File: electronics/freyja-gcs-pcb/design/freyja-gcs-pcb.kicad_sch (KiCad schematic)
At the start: 32 parts, among them J1 Conn_01x07_Pin, J2 GT-USB-7010ASV, SW1 SW_SPST, SW2 SW_SPST, U1 SN65HVD232DR, U2 STM32U575RGTx, Y1 48MHz, Y2 32768Hz

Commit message: 7 segment display
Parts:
- removed D3: LED Green, symbol Device:LED
- removed R3: 470, symbol Device:R
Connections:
- net 7SEG_SHCLK: now reaches U2.14 (PA0)
- net 7SEG_STCLK: now reaches U2.15 (PA1)
- net 7SEG_DA: now reaches U2.16 (PA2)
- net 7SEG_DIG1: now reaches U2.17 (PA3)
- net 7SEG_DIG2: now reaches U2.20 (PA4)
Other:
- sheet Switch_pins renamed Switches
- added sheet 7-Segment Display (7seg.kicad_sch)

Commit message: global reset
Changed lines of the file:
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@@
-	(wire
-		(pts
-			(xy 55.88 40.64) (xy 60.96 40.64)
-		)
-		(stroke
-			(width 0)
-			(type default)
-		)
-	)
 	(wire
 		(pts
@@
 		(pts
 			(xy 76.2 33.02) (xy 76.2 31.75)
+		)
+		(stroke
+			(width 0)
+			(type default)
+		)
+	)
+	(wire
+		(pts
+			(xy 59.69 40.64) (xy 60.96 40.64)
 		)
 		(stroke
@@
 	(label "USB_D_P"
 		(at 36.83 167.64 0)
-		(effects
-			(font
-				(size 1.27 1.27)
-			)
-			(justify left bottom)
-		)
-	)
-	(label "NRST"
-		(at 55.88 40.64 0)
 		(effects
 			(font
@@
 				(hide yes)
 			)
+		)
+	)
+	(global_label "NRST"
+		(shape output)
+		(at 59.69 40.64 180)
+		(fields_autoplaced yes)
+		(effects
+			(font
+				(size 1.27 1.27)
+			)
+			(justify right)
+		)
+		(property "Intersheetrefs" "${INTERSHEET_REFS}"
+			(at 51.9272 40.64 0)
+			(effects
+				(font
+					(size 1.27 1.27)
+				)
+				(justify right)
+				(hide yes)
+			)

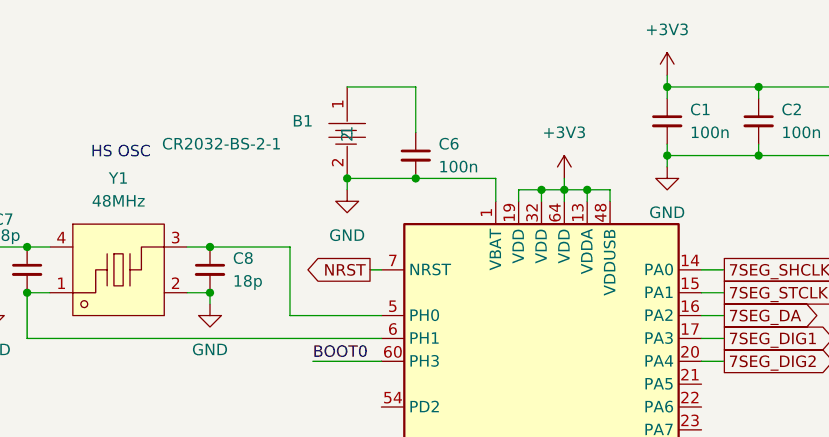
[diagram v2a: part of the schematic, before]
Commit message: fix cr2032 short circuit
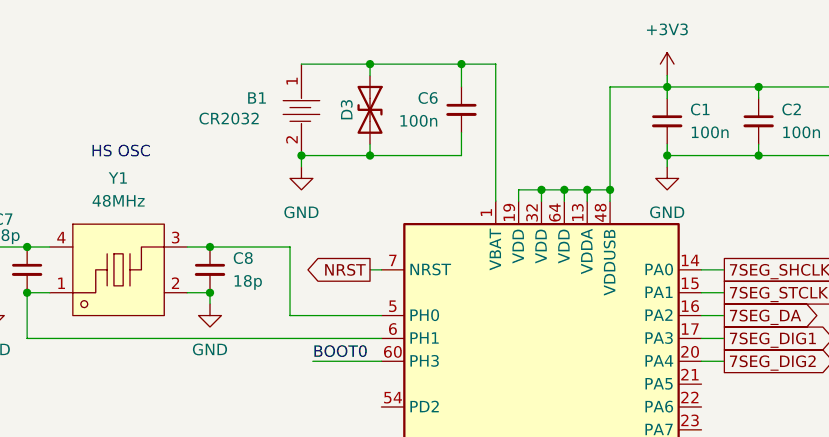
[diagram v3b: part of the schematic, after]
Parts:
- added D3: 0603ESDA-05N, Diode_SMD:D_0603_1608Metric_Pad1.05x0.95mm_HandSolder, symbol Device:D_TVS
- B1: value CR2032-BS-2-1 -> CR2032
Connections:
- net GND: now also D3.2 (A2); no longer U2.1 (VBAT)
- net at B1.1, C6.1: now also U2.1 (VBAT), D3.1 (A1)
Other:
- moved on the sheet: C6
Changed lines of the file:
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@@
 	)
 	(junction
-		(at 64.77 30.48)
+		(at 81.28 31.75)
 		(diameter 0)
 		(color 0 0 0 0)
 	)
 	(junction
-		(at 81.28 31.75)
+		(at 59.69 27.94)
+		(diameter 0)
+		(color 0 0 0 0)
+	)
+	(junction
+		(at 59.69 17.78)
 		(diameter 0)
 		(color 0 0 0 0)
@@
 	)
 	(junction
+		(at 69.85 17.78)
+		(diameter 0)
+		(color 0 0 0 0)
+	)
+	(junction
 		(at 41.91 38.1)
 		(diameter 0)
@@
 	)
 	(junction
+		(at 86.36 31.75)
+		(diameter 0)
+		(color 0 0 0 0)
+	)
+	(junction
 		(at 168.91 45.72)
 		(diameter 0)
@@
 	)
 	(junction
-		(at 57.15 30.48)
+		(at 52.07 27.94)
 		(diameter 0)
 		(color 0 0 0 0)
@@
 	(wire
 		(pts
-			(xy 73.66 33.02) (xy 73.66 30.48)
+			(xy 86.36 20.32) (xy 86.36 31.75)
+		)
+		(stroke
+			(width 0)
+			(type default)
+		)
+	)
+	(wire
+		(pts
+			(xy 73.66 17.78) (xy 73.66 33.02)
 		)
 		(stroke
@@
 	(wire
 		(pts
+			(xy 86.36 20.32) (xy 92.71 20.32)
+		)
+		(stroke
+			(width 0)
+			(type default)
+		)
+	)
+	(wire
+		(pts
 			(xy 123.19 20.32) (xy 123.19 21.59)
 		)
@@
 	(wire
 		(pts
+			(xy 59.69 17.78) (xy 52.07 17.78)
+		)
+		(stroke
+			(width 0)
+			(type default)
+		)
+	)
+	(wire
+		(pts
 			(xy 26.67 167.64) (xy 27.94 167.64)
 		)
@@
 	(wire
 		(pts
+			(xy 69.85 25.4) (xy 69.85 27.94)
+		)
+		(stroke
+			(width 0)
+			(type default)
+		)
+	)
+	(wire
+		(pts
 			(xy 36.83 106.68) (xy 43.18 106.68)
 		)
@@
 	(wire
 		(pts
-			(xy 73.66 30.48) (xy 64.77 30.48)
-		)
-		(stroke
-			(width 0)
-			(type default)
-		)
-	)
-	(wire
-		(pts
 			(xy 92.71 168.91) (xy 100.33 168.91)
 		)
@@
 	(wire
 		(pts
-			(xy 57.15 30.48) (xy 64.77 30.48)
+			(xy 52.07 27.94) (xy 59.69 27.94)
 		)
 		(stroke
@@
 	(wire
 		(pts
-			(xy 64.77 25.4) (xy 64.77 20.32)
+			(xy 69.85 17.78) (xy 69.85 20.32)
 		)
 		(stroke
@@
 	(wire
 		(pts
-			(xy 81.28 30.48) (xy 81.28 31.75)
+			(xy 59.69 26.67) (xy 59.69 27.94)
+		)
+		(stroke
+			(width 0)
+			(type default)
+		)
+	)
+	(wire
+		(pts
+			(xy 59.69 17.78) (xy 59.69 19.05)
+		)
+		(stroke
+			(width 0)
+			(type default)
+		)
+	)
+	(wire
+		(pts
+			(xy 69.85 17.78) (xy 73.66 17.78)
 		)
 		(stroke
@@
 	(wire
 		(pts
-			(xy 64.77 20.32) (xy 57.15 20.32)
+			(xy 59.69 17.78) (xy 69.85 17.78)
 		)
 		(stroke
@@
 	(wire
 		(pts
+			(xy 59.69 27.94) (xy 69.85 27.94)
+		)
+		(stroke
+			(width 0)
+			(type default)
+		)
+	)
+	(wire
+		(pts
 			(xy 179.07 54.61) (xy 179.07 55.88)
 		)
@@
 	(wire
 		(pts
-			(xy 57.15 30.48) (xy 57.15 31.75)
+			(xy 52.07 27.94) (xy 52.07 29.21)
 		)
 		(stroke
@@
 	(symbol
 		(lib_id "power:GND")
-		(at 57.15 31.75 0)
+		(at 52.07 29.21 0)
 		(unit 1)
 		(exclude_from_sim no)
@@
 		(fields_autoplaced yes)
 		(property "Reference" "#PWR05"
-			(at 57.15 38.1 0)
+			(at 52.07 35.56 0)
 			(effects
 				(font
@@
 		)
 		(property "Value" "GND"
-			(at 57.15 36.83 0)
+			(at 52.07 34.29 0)
 			(effects
 				(font
@@
 		)
 		(property "Footprint" ""
-			(at 57.15 31.75 0)
+			(at 52.07 29.21 0)
 			(effects
 				(font
@@
 		)
 		(property "Datasheet" ""
-			(at 57.15 31.75 0)
+			(at 52.07 29.21 0)
 			(effects
 				(font
@@
 		)
 		(property "Description" "Power symbol creates a global label with name \"GND\" , ground"
-			(at 57.15 31.75 0)
+			(at 52.07 29.21 0)
 			(effects
 				(font
@@
 	(symbol
 		(lib_id "EasyEDA:CR2032-BS-2-1")
-		(at 57.15 25.4 270)
+		(at 52.07 22.86 270)
 		(unit 1)
 		(exclude_from_sim no)
@@
 		(dnp no)
 		(property "Reference" "B1"
-			(at 51.054 24.13 90)
+			(at 45.974 21.59 90)
 			(effects
 				(font
@@
 			)
 		)
-		(property "Value" "CR2032-BS-2-1"
-			(at 36.576 26.67 90)
+		(property "Value" "CR2032"
+			(at 40.64 23.876 90)
 			(effects
 				(font
@@
 		)
 		(property "Footprint" "EasyEDA:BAT-TH_BS-2-1"
-			(at 49.53 25.4 0)
+			(at 44.45 22.86 0)
 			(effects
 				(font
@@
 		)
 		(property "Datasheet" "https://lcsc.com/product-detail/Battery-Holders-Clips-Contacts_CR2032battery_C70376.html"
-			(at 46.99 25.4 0)
+			(at 41.91 22.86 0)
 			(effects
 				(font
@@
 			)
 		)
-		(property "Description" ""
-			(at 57.15 25.4 0)
+		(property "Description" "CR2032-BS-2-1"
+			(at 52.07 22.86 0)
 			(effects
 				(font
@@
 		)
 		(property "LCSC Part" "C70376"
-			(at 44.45 25.4 0)
+			(at 39.37 22.86 0)
 			(effects
 				(font
@@
 	)
 	(symbol
+		(lib_id "Device:D_TVS")
+		(at 59.69 22.86 270)
+		(unit 1)
+		(exclude_from_sim no)
+		(in_bom yes)
+		(on_board yes)
+		(dnp no)
+		(property "Reference" "D3"
+			(at 57.15 22.86 0)
+			(effects
+				(font
+					(size 1.27 1.27)
+				)
+			)
+		)
+		(property "Value" "0603ESDA-05N"
+			(at 57.15 21.5901 90)
+			(effects
+				(font
+					(size 1.27 1.27)
+				)
+				(justify right)
+				(hide yes)
+			)
+		)
+		(property "Footprint" "Diode_SMD:D_0603_1608Metric_Pad1.05x0.95mm_HandSolder"
+			(at 59.69 22.86 0)
+			(effects
+				(font
+					(size 1.27 1.27)
+				)
+				(hide yes)
+			)
+		)
+		(property "Datasheet" "~"
+			(at 59.69 22.86 0)
+			(effects
+				(font
+					(size 1.27 1.27)
+				)
+				(hide yes)
+			)
+		)
+		(property "Description" "Bidirectional transient-voltage-suppression diode"
+			(at 59.69 22.86 0)
+			(effects
+				(font
+					(size 1.27 1.27)
+				)
+				(hide yes)
+			)
+		)
+		(property "LCSC Part" "C316054"
+			(at 46.99 22.86 0)
+			(effects
+				(font
+					(size 1.27 1.27)
+				)
+				(hide yes)
+			)
+		)
+		(pin "1"
+		)
+		(pin "2"
+		)
+		(instances
+			(project "freyja-gcs-pcb"
+				(path "/c292fa04-82ad-49e9-a9d8-422554d1d11d"
+					(reference "D3")
+					(unit 1)
+				)
+			)
+		)
+	)
+	(symbol
 		(lib_id "Device:R")
 		(at 31.75 157.48 90)
@@
 	(symbol
 		(lib_id "Device:C_Small")
-		(at 64.77 27.94 0)
+		(at 69.85 22.86 0)
+		(mirror y)
 		(unit 1)
 		(exclude_from_sim no)
@@
 		(on_board yes)
 		(dnp no)
-		(fields_autoplaced yes)
 		(property "Reference" "C6"
-			(at 67.31 26.6762 0)
+			(at 67.31 21.59 0)
 			(effects
 				(font
@@
 		)
 		(property "Value" "100n"
-			(at 67.31 29.2162 0)
+			(at 67.31 24.13 0)
 			(effects
 				(font
@@
 		)
 		(property "Footprint" ""
-			(at 64.77 27.94 0)
+			(at 69.85 22.86 0)
 			(effects
 				(font
@@
 		)
 		(property "Datasheet" "~"
-			(at 64.77 27.94 0)
+			(at 69.85 22.86 0)
 			(effects
 				(font
@@
 		)
 		(property "Description" "Unpolarized capacitor, small symbol"
-			(at 64.77 27.94 0)
+			(at 69.85 22.86 0)
 			(effects
 				(font
@@
 					(unit 1)
 				)
-			)
-		)
-	)
-	(symbol
-		(lib_id "power:+3V3")
-		(at 81.28 30.48 0)
-		(unit 1)
-		(exclude_from_sim no)
-		(in_bom yes)
-		(on_board yes)
-		(dnp no)
-		(fields_autoplaced yes)
-		(property "Reference" "#PWR03"
-			(at 81.28 34.29 0)
-			(effects
-				(font
-					(size 1.27 1.27)
-				)
-				(hide yes)
-			)
-		)
-		(property "Value" "+3V3"
-			(at 81.28 25.4 0)
-			(effects
-				(font
-					(size 1.27 1.27)
-				)
-			)
-		)
-		(property "Footprint" ""
-			(at 81.28 30.48 0)
-			(effects
-				(font
-					(size 1.27 1.27)
-				)
-				(hide yes)
-			)
-		)
-		(property "Datasheet" ""
-			(at 81.28 30.48 0)
-			(effects
-				(font
-					(size 1.27 1.27)
-				)
-				(hide yes)
-			)
-		)
-		(property "Description" "Power symbol creates a global label with name \"+3V3\""
-			(at 81.28 30.48 0)
-			(effects
-				(font
-					(size 1.27 1.27)
-				)
-				(hide yes)
-			)
-		)
-		(pin "1"
-		)
-		(instances
-			(project ""
-				(path "/c292fa04-82ad-49e9-a9d8-422554d1d11d"
-					(reference "#PWR03")
-					(unit 1)
-				)

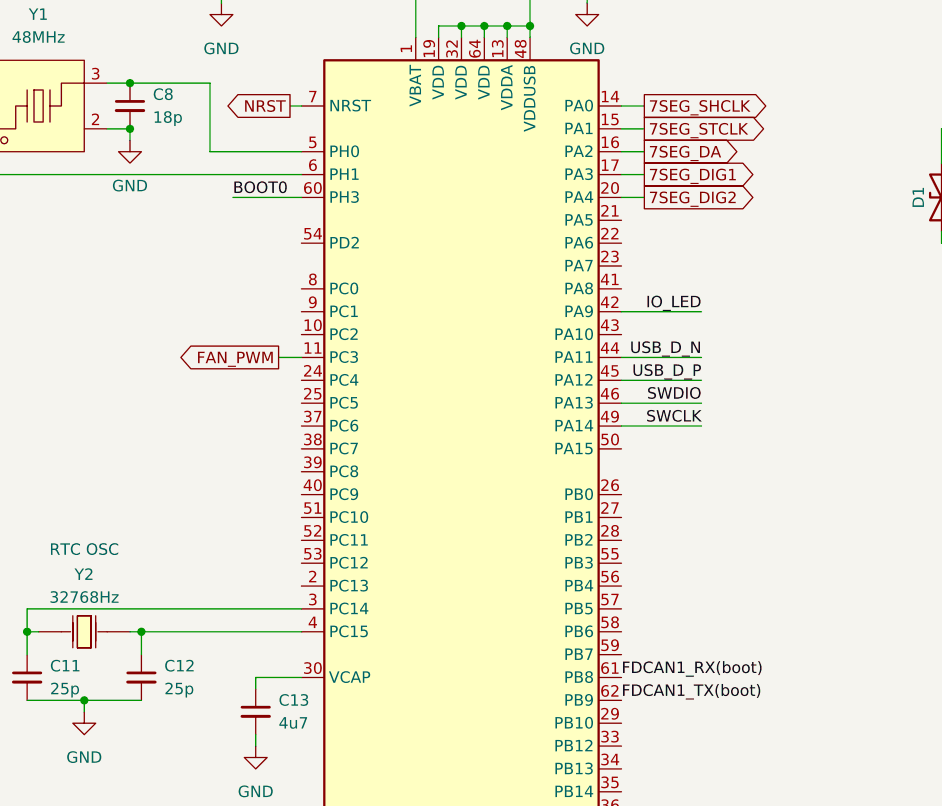
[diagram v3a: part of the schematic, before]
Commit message: change pwm channels
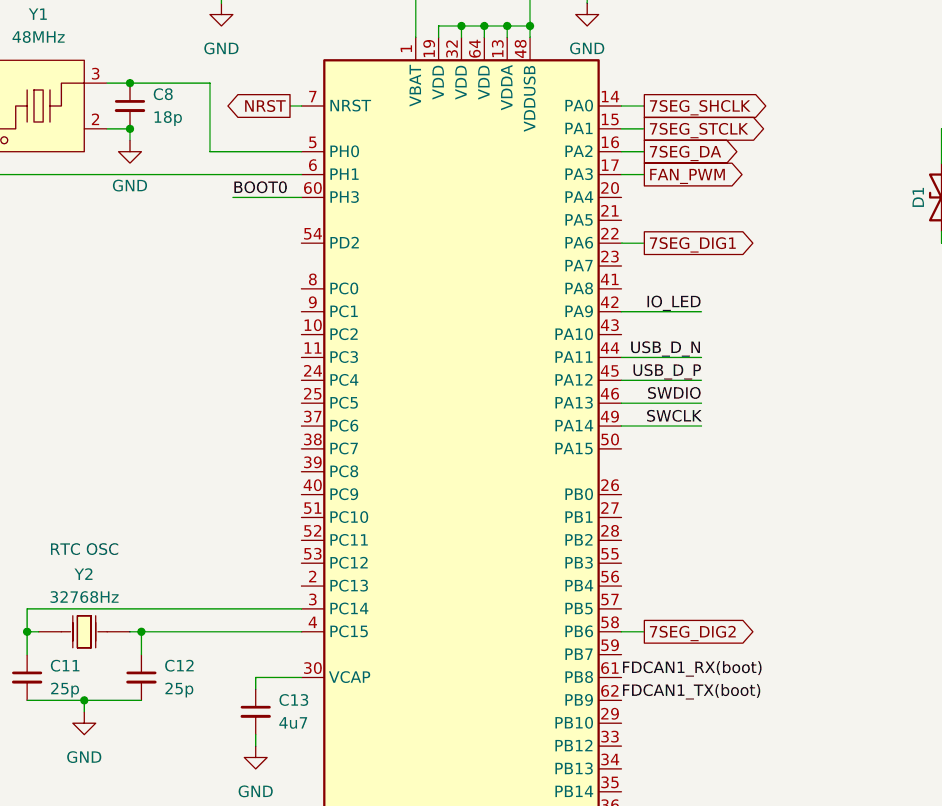
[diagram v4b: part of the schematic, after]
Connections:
- net 7SEG_DIG1: now also U2.22 (PA6); no longer U2.17 (PA3)
- net 7SEG_DIG2: now also U2.58 (PB6); no longer U2.20 (PA4)
- net FAN_PWM: now also U2.17 (PA3); no longer U2.11 (PC3)

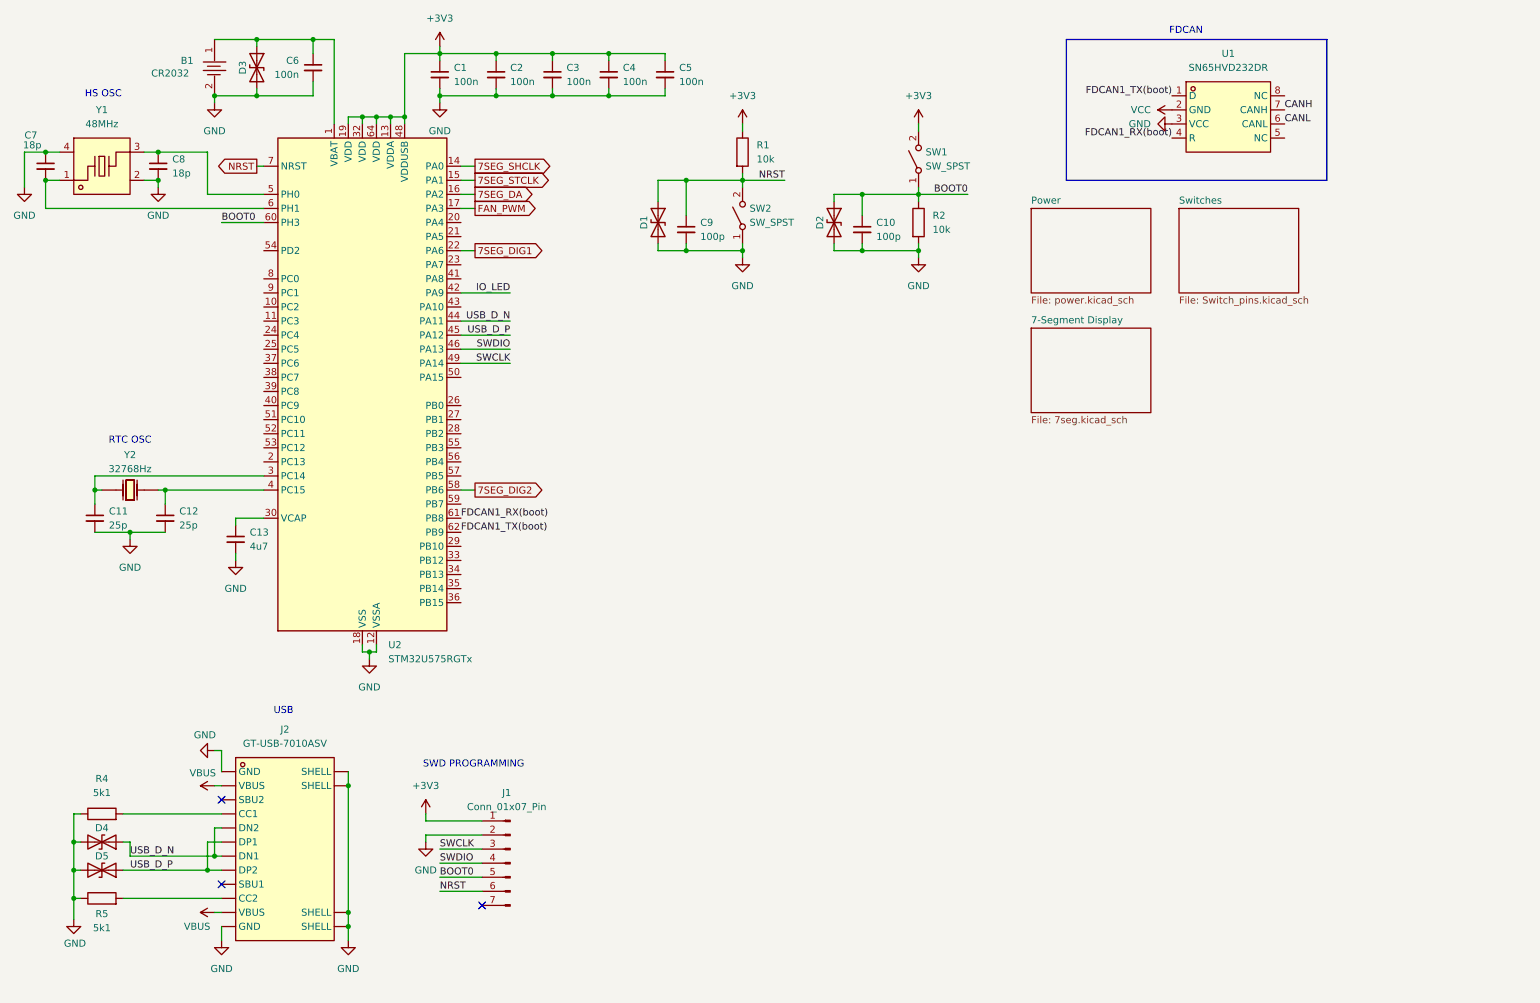
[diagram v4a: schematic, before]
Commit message: add can connectors
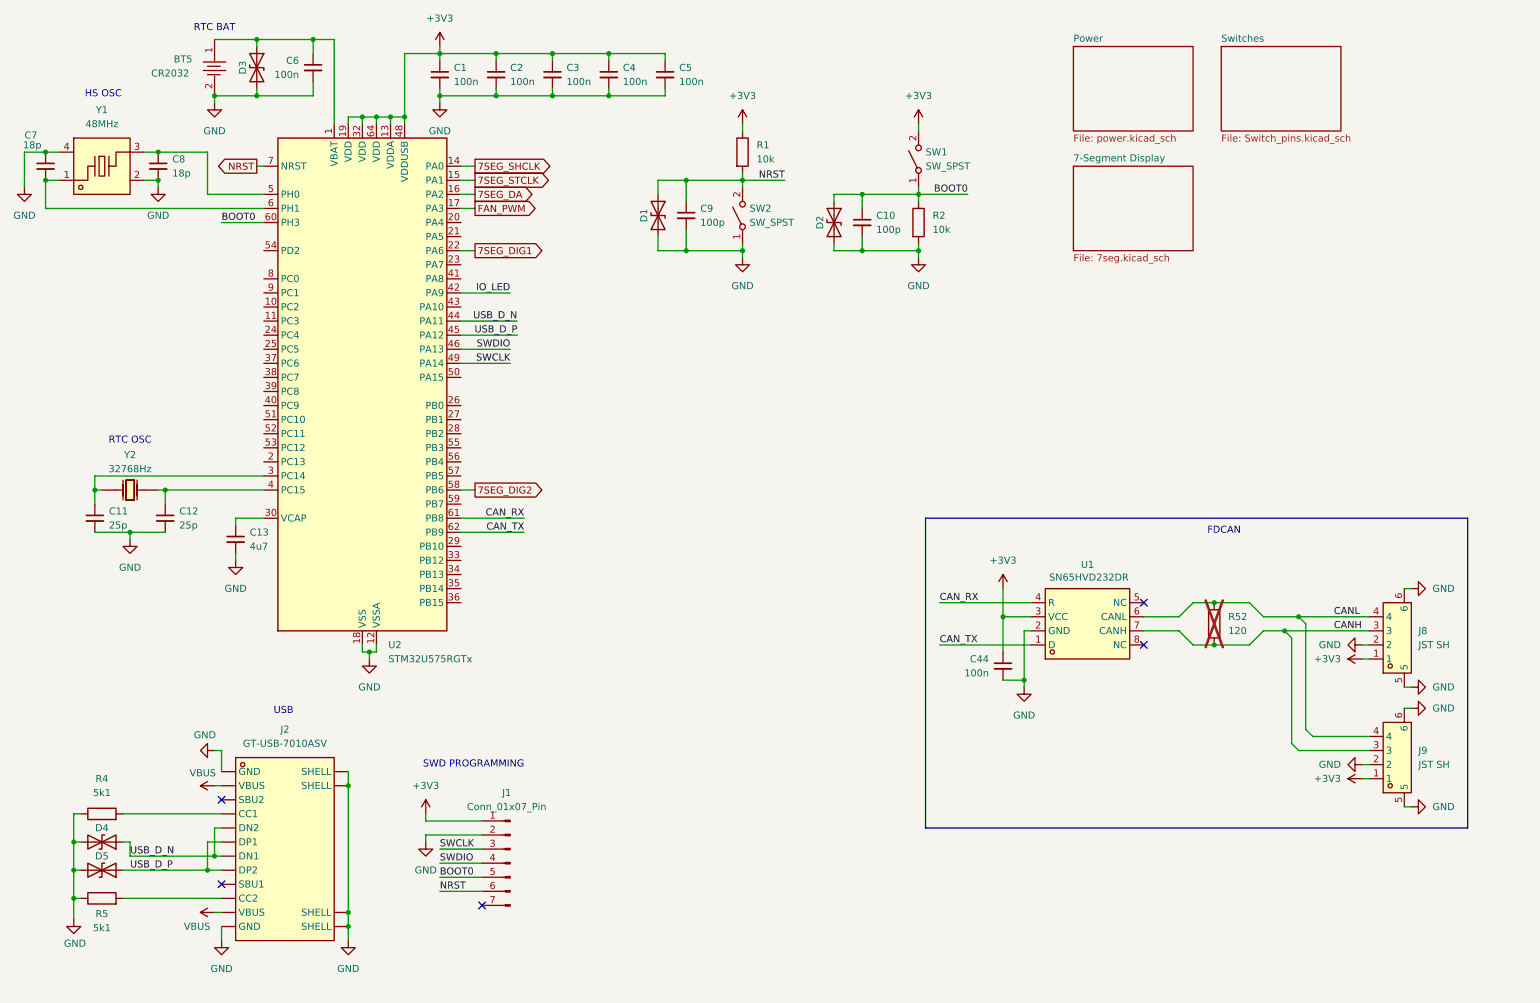
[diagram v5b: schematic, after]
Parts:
- added C44: 100n, symbol Device:C_Small
- added J8, J9: JST SH, EasyEDA:CONN-SMD_AFC10-S04QCA-00, symbol EasyEDA:AFC10-S04QCA-00
- added R52: 120, symbol Device:R
- renumbered B1 to BT5
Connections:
- net VCC is gone; now on net GND: U1.2 (GND)
- net +3V3: now also U1.3 (VCC), C44.1, J8.1, J9.1
- net CANH: now also J8.3, J9.3, R52.1
- net CANL: now also J8.4, J9.4, R52.2
- net GND: now also C44.2, J8.2, J8.5, J8.6, J9.2, J9.5, J9.6; no longer U1.3 (VCC)
- net FDCAN1_RX(boot) renamed CAN_RX
- net FDCAN1_TX(boot) renamed CAN_TX
- no-connect marks 3 -> 5
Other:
- note added: "RTC BAT"
- moved on the sheet: C10, C9, D1, U1

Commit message: buttons and indicators
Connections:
- net TGL0_LED: now reaches U2.10 (PC2)
- net TGL1: now reaches U2.11 (PC3)
- net TGL1_LED: now reaches U2.24 (PC4)
- net TGL2: now reaches U2.25 (PC5)
- net AUX_BTN: now reaches U2.26 (PB0)
- net LAUNCH_ARMD_LED: now reaches U2.27 (PB1)
- net CMD_ARMD_LED: now reaches U2.28 (PB2)
- net AUX_LED: now reaches U2.29 (PB10)
- net TGL6: now reaches U2.33 (PB12)
- net TGL6_LED: now reaches U2.34 (PB13)
- net TGL7: now reaches U2.35 (PB14)
- net TGL7_LED: now reaches U2.36 (PB15)
- net TGL2_LED: now reaches U2.37 (PC6)
- net TGL3: now reaches U2.38 (PC7)
- net TGL3_LED: now reaches U2.39 (PC8)
- net TGL4: now reaches U2.40 (PC9)
- net LAUNCH_ARMD: now reaches U2.41 (PA8)
- net CMD_ARMD: now reaches U2.43 (PA10)
- net CMD_SEND: now reaches U2.50 (PA15)
- net TGL4_LED: now reaches U2.51 (PC10)
- net TGL5: now reaches U2.52 (PC11)
- net TGL5_LED: now reaches U2.53 (PC12)
- net FAULT_LED: now reaches U2.55 (PB3)
- net CON_STS_RKT: now reaches U2.56 (PB4)
- net CON_STS_LPD: now reaches U2.57 (PB5)
- net LAUNCHED_LED: now reaches U2.59 (PB7)
- net TGL0: now reaches U2.9 (PC1)
- net IO_LED renamed LAUNCH
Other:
- sheet Switches renamed Switches & indicators
